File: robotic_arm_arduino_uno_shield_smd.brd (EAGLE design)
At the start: 44.5 x 53.3 mm, 39 parts, among them J1 (ID,OD)=(2.1,5.5)MM

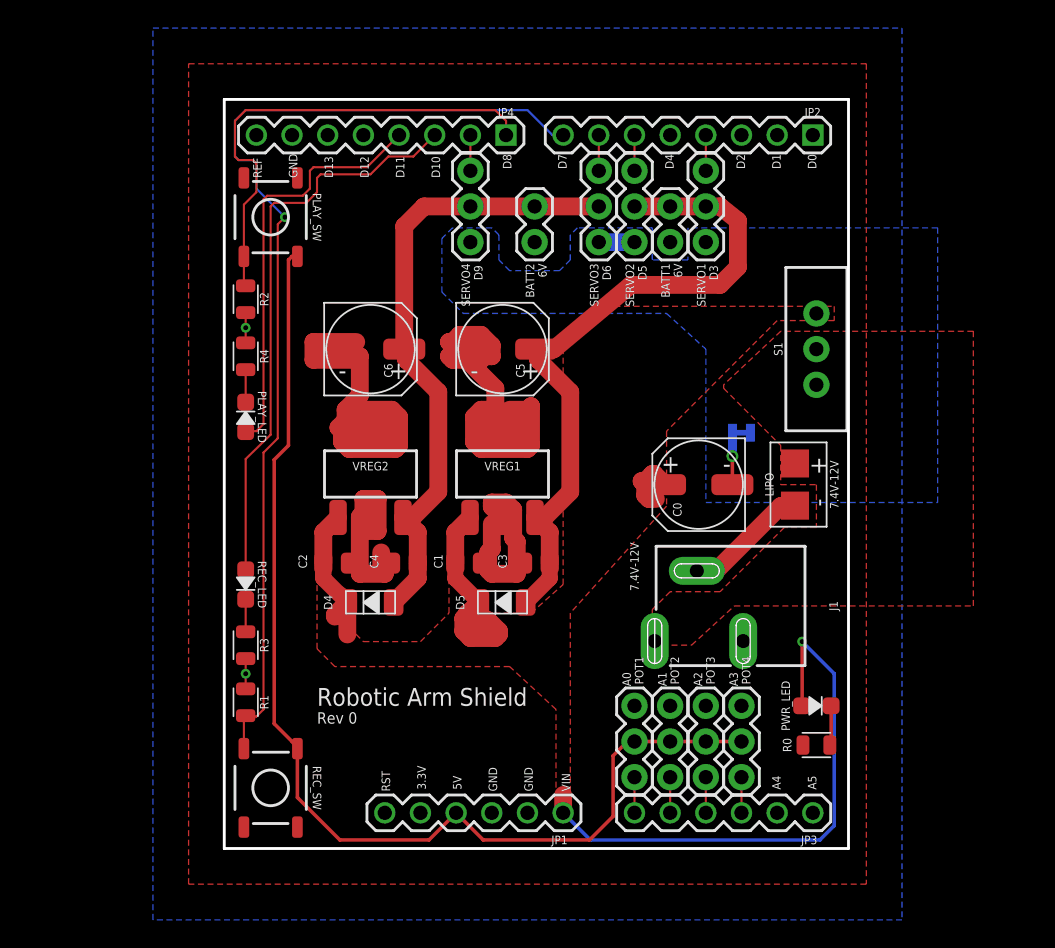
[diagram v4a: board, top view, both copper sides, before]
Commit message: Rev 2.  Changed pad sizes of 805 SMD components.
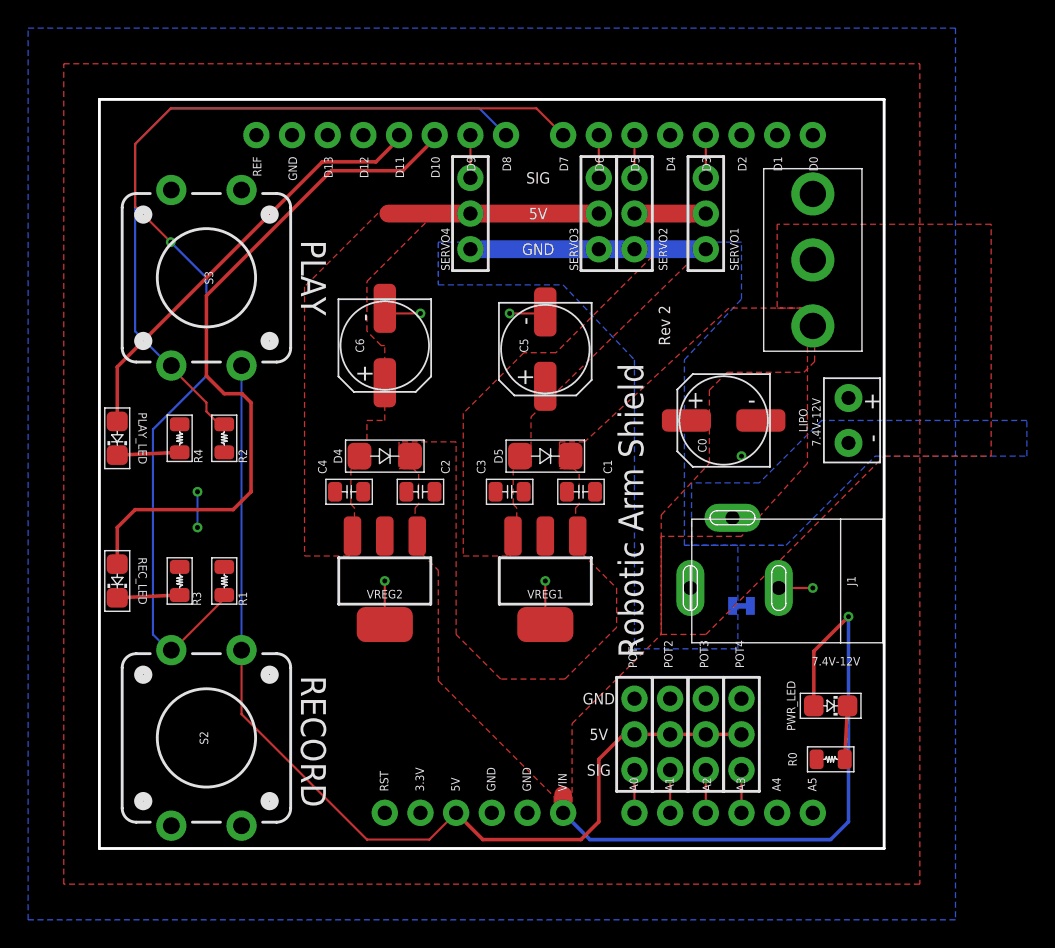
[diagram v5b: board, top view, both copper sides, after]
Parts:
- removed BATT1, BATT2: 6V, SparkFun-Connectors:1X02
- removed JP1: Power, SparkFun:1X06
- removed JP2: Digital1, SparkFun:1X08
- removed JP3: Analog, SparkFun:1X06
- removed JP4: Digital2, SparkFun:1X08
- removed PLAY_SW, REC_SW: TACTILE-SW_500mA/12V, MrSwirlyEyes:SW_MOMENTARY_SPST-NO_SMD_12V_50MA_5.2MM
- added J2, J3: 1x06-VERT-MALE, connectors:1X06-VERT-MALE
- added J4, J5: 1x08-VERT-MALE, connectors:1X08-VERT-MALE
- added S2, S3: MOMENTARY-SWITCH-SPST-PTH-12MM, SparkFun-Switches:TACTILE_SWITCH_PTH_12MM
- C0, C5, C6: device MrSwirlyEyes:CAP_POL_ALUM-ELECTROLYTIC -> MrSwirlyEyes:CAP_POL_SMD_L6.6-W6.6
- LIPO: value BATTERY -> BATTERYPTH_HOLES; device MrSwirlyEyes:DUAL_SMD_PADS -> MrSwirlyEyes:DUAL_PTH_PADS
- POT1, POT2, POT3, POT4: value 22K -> 1x03-VERT-FEMALE; device SparkFun-Connectors:1X03 -> connectors:1X03-VERT-FEMALE
- S1: device SparkFun-Switches:SWITCH_SPDT_PTH_11.6X4.0MM -> MrSwirlyEyes:SW-SLIDE_SPDT_5A-28V_13L-7W
- SERVO1, SERVO2, SERVO3, SERVO4: value (none) -> 1x03-VERT-FEMALE; device SparkFun-Connectors:1X03 -> connectors:1X03-VERT-FEMALE
- moved SUPPLY14 12.3 mm to (36.8, 17.3), turned to 270 degrees
- moved D5 10.9 mm to (22.9, 27.9), turned to 0 degrees
- moved D4 10.5 mm to (11.4, 27.9), turned to 0 degrees
- moved R2 10.0 mm to (0.00, 29.2)
- moved C1 9.48 mm to (25.4, 25.4), turned to 180 degrees
- moved PLAY_LED 9.27 mm to (-7.62, 29.2), turned to 270 degrees
- moved REC_LED 9.15 mm to (-7.62, 19.1)
- moved R1 8.77 mm to (0.00, 19.1)
- moved VREG1 8.21 mm to (22.9, 19.1), turned to 180 degrees
- moved C2 7.84 mm to (14.0, 25.4), turned to 180 degrees
- moved VREG2 7.69 mm to (11.4, 19.1), turned to 180 degrees
- moved R4 7.50 mm to (-3.17, 29.2)
- moved R3 6.56 mm to (-3.17, 19.1), turned to 270 degrees
- moved C4 6.43 mm to (8.89, 25.4), turned to 0 degrees
- moved S1 6.36 mm to (41.9, 41.9), turned to 90 degrees
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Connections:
- removed net N$6: J1.GND@2, LIPO.V-
- removed net VBATT: J1.PWR, LIPO.V+, S1.2
- new net +: J1.PWR, LIPO.+, S1.P$2
- new net -: J1.GND@2, LIPO.-
- net 3.3V: now also J2.2; no longer JP1.2
- net 5V: now also J2.3, S2.1, S3.3; no longer JP1.3, PLAY_SW.3, REC_SW.1
- net A0: now also J3.6; no longer JP3.6
- net A1: now also J3.5; no longer JP3.5
- net A2: now also J3.4; no longer JP3.4
- net A3: now also J3.3; no longer JP3.3
- net A4: now also J3.2; no longer JP3.2
- net A5: now also J3.1; no longer JP3.1
- net AREF: now also J5.8; no longer JP4.8
- net D10: now also J5.3; no longer JP4.3
- net D11: now also J5.4; no longer JP4.4
- net D12: now also J5.5; no longer JP4.5
- net D13: now also J5.6; no longer JP4.6
- net D2: now also J4.3; no longer JP2.3
- net D3: now also J4.4; no longer JP2.4
- net D4: now also J4.5; no longer JP2.5
- net D5: now also J4.6; no longer JP2.6
- net D6: now also J4.7; no longer JP2.7
- net D7: now also J4.8, S2.3; no longer JP2.8, REC_SW.3
- net D8: now also J5.1, S3.1; no longer JP4.1, PLAY_SW.1
- net D9: now also J5.2; no longer JP4.2
- net GND: now also J2.4, J2.5, J5.7; no longer BATT1.2, BATT2.2, JP1.4, JP1.5, JP4.7
- net RESET: now also J2.1; no longer JP1.1
- net RX: now also J4.1; no longer JP2.1
- net TX: now also J4.2; no longer JP2.2
- net VCC_1: no longer BATT1.1
- net VCC_2: no longer BATT2.1
- net VIN: now also J2.6, S1.P$1; no longer JP1.6, S1.1
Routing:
- net GND: track 91.0 -> 17.3 mm, vias 3 -> 8
- net VCC_1: track 49.2 -> 5.08 mm
- net VCC_2: track 44.8 -> 15.0 mm
- net VIN: track 73.5 -> 44.9 mm
- net D8: track 34.6 -> 51.5 mm
- net NGND: track 2.54 -> 16.8 mm
- net D10: track 41.0 -> 50.4 mm
- net N$6: track 8.91 -> 0.00 mm
- net 5V: track 80.0 -> 71.6 mm
- net D7: track 72.9 -> 78.4 mm
- net N$2: track 2.31 -> 4.45 mm
- net N$1: track 2.31 -> 4.45 mm
- net D11: track 29.8 -> 30.9 mm
- net N$4: track 2.81 -> 3.82 mm
- net A3: track 2.54 -> 3.05 mm
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- added copper zone on layer 1, net +
- added copper zone on layer 16, net -
- added copper zone on layer 1, net VCC_1
- added copper zone on layer 1, net VCC_2
- removed copper zone on layer 1, net VBATT
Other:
- board size 44.5 x 53.3 mm -> 55.9 x 53.3 mm
- board text added: "PLAY"
- board text added: "RECORD"
- board text added: "Rev 2"
- board text added: "Rev 2 Designed by: Buu Truong CADed by: MrSwirlyEyes"
- board text added: "SIG"
- board text removed: "6V"
- board text removed: "CADed by: MrSwirlyEyes"
- board text removed: "Designed by: Buu Truong"
- board text removed: "Rev 0"

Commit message: Added switch object parameters for power switch and PLAY,RECORD buttons.  Added potentiometer from digikey to POT object.  Added Servo from Amazon to SERVO object MG90S
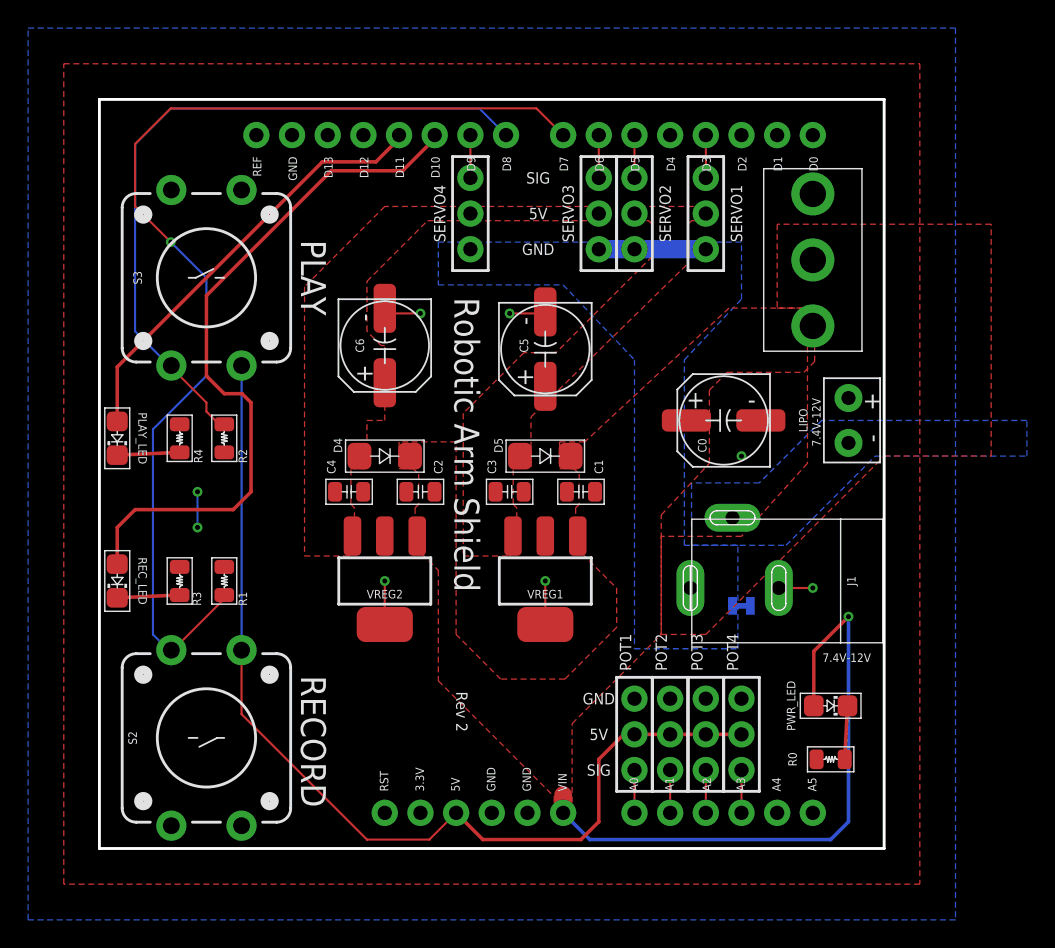
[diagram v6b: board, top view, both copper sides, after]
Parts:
- POT1, POT2, POT3, POT4: value 1x03-VERT-FEMALE -> 20KΩ; device connectors:1X03-VERT-FEMALE -> MrSwirlyEyes:CONNECTOR_POTENTIOMETER_NO-MARKINGS_FEMALE-HEADER
- R3: value 10KΩ -> 2KΩ
- R4: value 10KΩ -> 1KΩ
- S1: value (none) -> 5A/28V
- S2, S3: value MOMENTARY-SWITCH-SPST-PTH-12MM -> (none); device SparkFun-Switches:TACTILE_SWITCH_PTH_12MM -> MrSwirlyEyes:SPST-PTH-12MM
- SERVO1, SERVO2, SERVO3, SERVO4: value 1x03-VERT-FEMALE -> MG90S; device connectors:1X03-VERT-FEMALE -> MrSwirlyEyes:CONNECTOR_SERVO_NO-MARKINGS
- turned POT1 to 90 degrees
- turned POT2 to 90 degrees
- turned POT3 to 90 degrees
- turned POT4 to 90 degrees
- turned SERVO1 to 270 degrees
- turned SERVO2 to 270 degrees
- turned SERVO3 to 270 degrees
- turned SERVO4 to 270 degrees
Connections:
- net 5V: now also POT1.CCW, POT2.CCW, POT3.CCW, POT4.CCW; no longer POT1.2, POT2.2, POT3.2, POT4.2
- net A0: now also POT1.S; no longer POT1.3
- net A1: now also POT2.S; no longer POT2.3
- net A2: now also POT3.S; no longer POT3.3
- net A3: now also POT4.S; no longer POT4.3
- net D3: now also SERVO1.1; no longer SERVO1.3
- net D5: now also SERVO2.1; no longer SERVO2.3
- net D6: now also SERVO3.1; no longer SERVO3.3
- net D9: now also SERVO4.1; no longer SERVO4.3
- net GND: now also POT1.CW, POT2.CW, POT3.CW, POT4.CW; no longer POT1.1, POT2.1, POT3.1, POT4.1
- net NGND: now also SERVO1.3, SERVO2.3, SERVO3.3, SERVO4.3; no longer SERVO1.1, SERVO2.1, SERVO3.1, SERVO4.1
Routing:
- net VCC_2: track 15.0 -> 0.00 mm
- net VCC_1: track 5.08 -> 0.00 mm
- net NGND: track 16.8 -> 15.2 mm

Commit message: Rev 2.  Modified board and schematic for new parts
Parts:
- S2, S3: value (none) -> 50mA/12V
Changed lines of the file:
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@@
 <attribute name="VALUE" value="5A/28V" x="41.91" y="41.91" size="1.778" layer="27" rot="R90" display="off"/>
 </element>
-<element name="S2" library="MrSwirlyEyes" package="SPST-PTH-12MM" value="" x="-1.27" y="7.874" smashed="yes" rot="R90">
+<element name="S2" library="MrSwirlyEyes" package="SPST-PTH-12MM" value="50mA/12V" x="-1.27" y="7.874" smashed="yes" rot="R90">
+<attribute name="CREATOR" value="MrSwirlyEyes" x="-1.27" y="7.874" size="1.778" layer="27" rot="R90" display="off"/>
+<attribute name="DATASHEET" value="https://www.sparkfun.com/datasheets/Components/Buttons/TSA12110%20TACT%20SWITCH.jpg" x="-1.27" y="7.874" size="1.778" layer="27" rot="R90" display="off"/>
+<attribute name="DIST" value="Sparkfun" x="-1.27" y="7.874" size="1.778" layer="27" rot="R90" display="off"/>
+<attribute name="DISTLINK" value="https://www.sparkfun.com/products/10302" x="-1.27" y="7.874" size="1.778" layer="27" rot="R90" display="off"/>
+<attribute name="DISTPN" value="COM-10302" x="-1.27" y="7.874" size="1.778" layer="27" rot="R90" display="off"/>
+<attribute name="MFR" value="" x="-1.27" y="7.874" size="1.778" layer="27" rot="R90" display="off"/>
+<attribute name="MPN" value="" x="-1.27" y="7.874" size="1.778" layer="27" rot="R90" display="off"/>
 <attribute name="NAME" x="-6.223" y="7.874" size="0.6096" layer="25" font="vector" ratio="20" rot="R90" align="bottom-center"/>
+<attribute name="VALUE" value="50mA/12V" x="-1.27" y="7.874" size="1.778" layer="27" rot="R90" display="off"/>
 </element>
-<element name="S3" library="MrSwirlyEyes" package="SPST-PTH-12MM" value="" x="-1.27" y="40.64" smashed="yes" rot="R270">
+<element name="S3" library="MrSwirlyEyes" package="SPST-PTH-12MM" value="50mA/12V" x="-1.27" y="40.64" smashed="yes" rot="R270">
+<attribute name="CREATOR" value="MrSwirlyEyes" x="-1.27" y="40.64" size="1.778" layer="27" rot="R270" display="off"/>
+<attribute name="DATASHEET" value="https://www.sparkfun.com/datasheets/Components/Buttons/TSA12110%20TACT%20SWITCH.jpg" x="-1.27" y="40.64" size="1.778" layer="27" rot="R270" display="off"/>
+<attribute name="DIST" value="Sparkfun" x="-1.27" y="40.64" size="1.778" layer="27" rot="R270" display="off"/>
+<attribute name="DISTLINK" value="https://www.sparkfun.com/products/10302" x="-1.27" y="40.64" size="1.778" layer="27" rot="R270" display="off"/>
+<attribute name="DISTPN" value="COM-10302" x="-1.27" y="40.64" size="1.778" layer="27" rot="R270" display="off"/>
+<attribute name="MFR" value="" x="-1.27" y="40.64" size="1.778" layer="27" rot="R270" display="off"/>
+<attribute name="MPN" value="" x="-1.27" y="40.64" size="1.778" layer="27" rot="R270" display="off"/>
 <attribute name="NAME" x="-6.477" y="40.64" size="0.6096" layer="25" font="vector" ratio="20" rot="R270" align="bottom-center"/>
+<attribute name="VALUE" value="50mA/12V" x="-1.27" y="40.64" size="1.778" layer="27" rot="R270" display="off"/>
 </element>
 <element name="SERVO1" library="MrSwirlyEyes" package="CONNECTOR_SERVO_NO-MARKINGS" value="MG90S" x="34.29" y="45.212" smashed="yes" rot="R270">

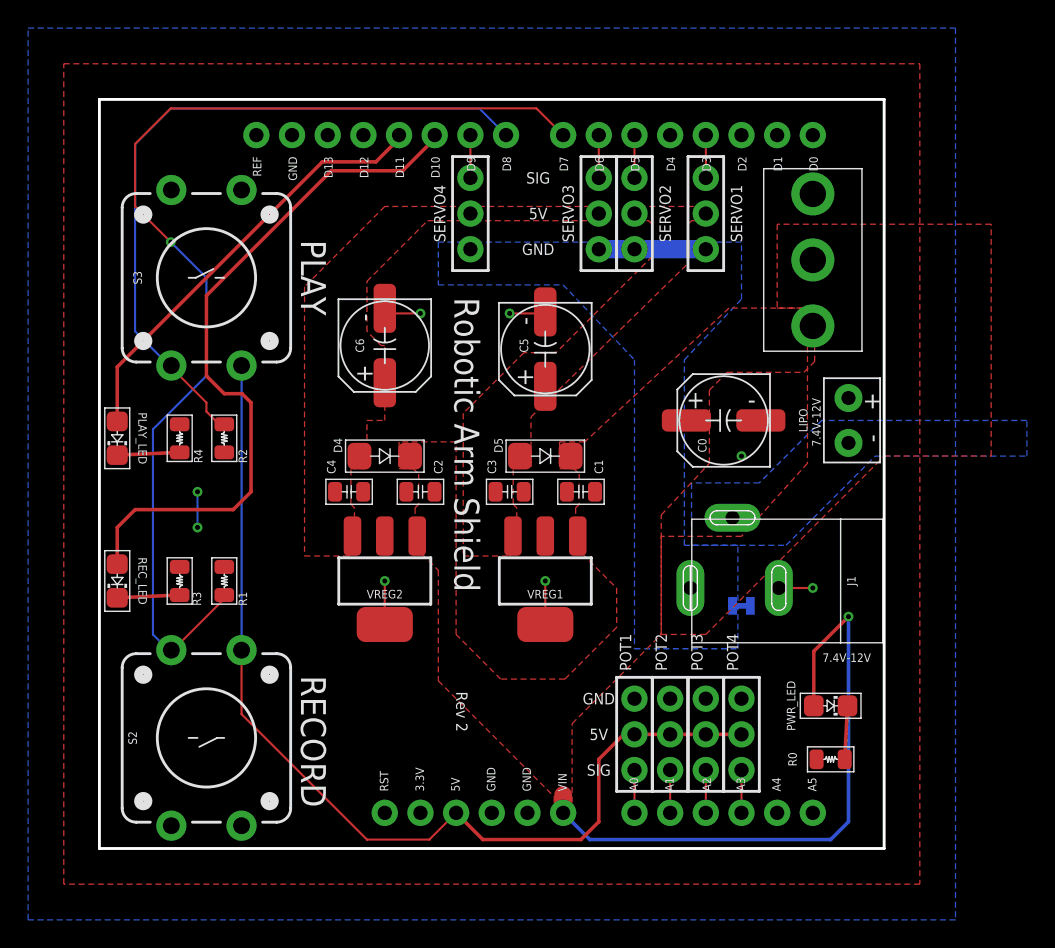
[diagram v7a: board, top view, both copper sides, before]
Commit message: Rev 3:  Complete revamp.  Replaced the (2) 1A/5V VREGs for (1) 5A/5V VREG
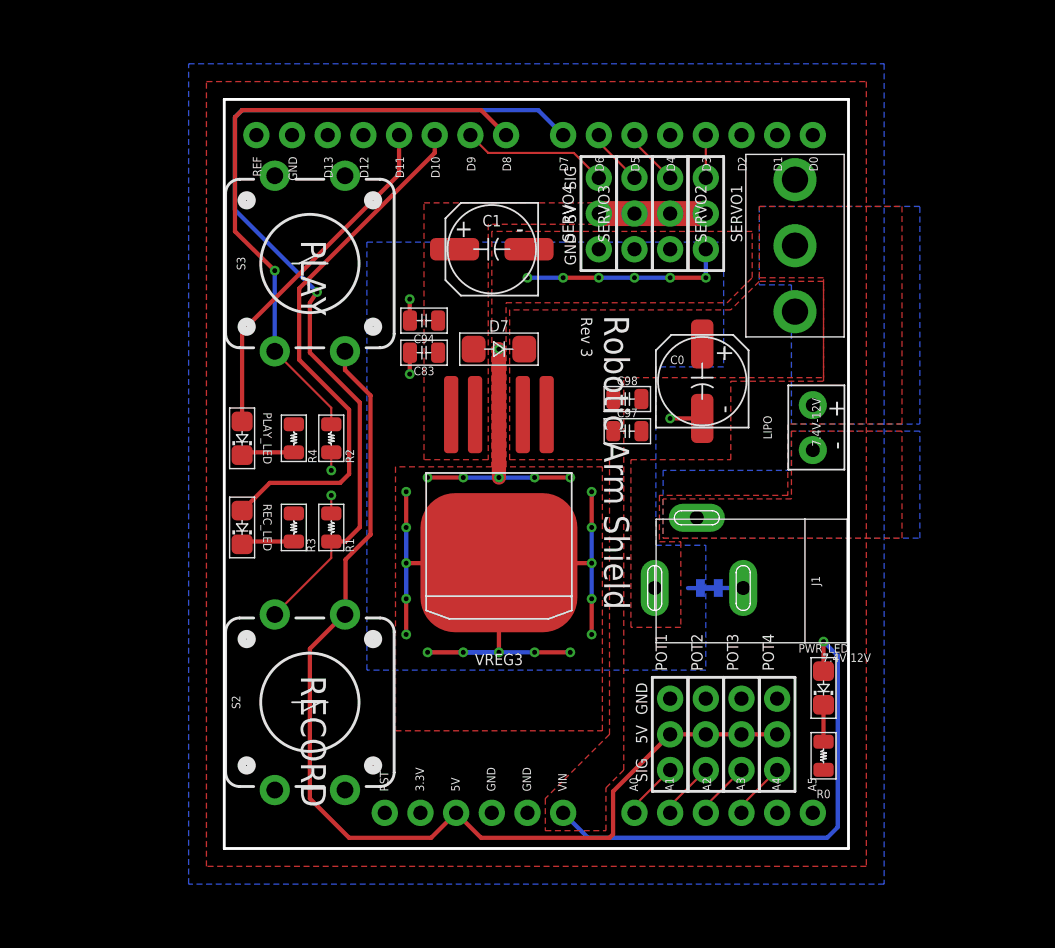
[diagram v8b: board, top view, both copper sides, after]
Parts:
- removed C2: 0.22uF/50V, MrSwirlyEyes:CAP_CER_SMD-805
- removed C3, C4: 0.1uF/50V, MrSwirlyEyes:CAP_CER_SMD-805
- removed C5, C6: 100UF/16V, MrSwirlyEyes:CAP_POL_SMD_L6.6-W6.6
- removed D4, D5: 1A/50V, MrSwirlyEyes:DIODE_SMD_1A-50V-SOD123F
- removed VREG1, VREG2: 1.5A/5V, MrSwirlyEyes:SOT223
- added C83, C98: 0.1uF/50V, MrSwirlyEyes:CAP_CER_SMD-805
- added C94, C97: 10uF/25V, MrSwirlyEyes:CAP_CER_SMD-805
- added D7: 1A/50V, MrSwirlyEyes:DIODE_SMD_1A-50V-SOD123F
- added VREG3: 5A/5V, MrSwirlyEyes:TO-263-5
- C1: value 0.22uF/50V -> 100UF/16V; device MrSwirlyEyes:CAP_CER_SMD-805 -> MrSwirlyEyes:CAP_POL_SMD_L6.6-W6.6
- R0, R1, R2, R3, R4: device MrSwirlyEyes:RESC2012X60_HS -> MrSwirlyEyes:RESISTOR_SMD-805
- moved C1 18.4 mm to (19.1, 42.7), turned to 0 degrees
- moved REC_LED 9.67 mm to (1.27, 22.9)
- moved SERVO4 9.14 mm to (26.7, 45.2)
- moved R3 8.98 mm to (4.95, 22.9)
- moved PLAY_LED 8.89 mm to (1.27, 29.2)
- moved R1 8.52 mm to (7.62, 22.9)
- moved R4 8.13 mm to (4.95, 29.2)
- moved S2 7.79 mm to (6.10, 10.4)
- moved R2 7.62 mm to (7.62, 29.2)
- moved S3 7.44 mm to (6.10, 41.7)
- moved C0 3.18 mm to (34.0, 33.3), turned to 270 degrees
- moved SUPPLY14 2.62 mm to (34.5, 18.6)
- moved LIPO 2.59 mm to (41.9, 30.0)
- moved J1 2.54 mm to (36.8, 19.1)
- moved POT1 2.54 mm to (31.8, 8.13)
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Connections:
- removed net VCC_1: C3.1, C5.A, D5.A, SERVO1.2, SERVO2.2, VREG1.3
- removed net VCC_2: C4.1, C6.A, D4.A, SERVO3.2, SERVO4.2, VREG2.3
- new net VCC: C1.A, C83.1, C94.1, D7.A, SERVO1.2, SERVO2.2, SERVO3.2, SERVO4.2, VREG3.4
- net GND: now also C97.2, C98.2; no longer C1.2, C2.2, C3.2, C4.2, C5.K, C6.K, VREG1.2, VREG1.4, VREG2.2, VREG2.4
- net NGND: now also C1.K, C83.2, C94.2, VREG3.3, VREG3.TAB
- net VIN: now also C97.1, C98.1, D7.K, VREG3.1, VREG3.2; no longer C1.1, C2.1, D4.K, D5.K, VREG1.1, VREG2.1
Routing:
- net NGND: track 15.2 -> 93.2 mm, vias 0 -> 29
- net D10: track 50.4 -> 38.3 mm
- net D7: track 78.4 -> 66.9 mm
- net GND: track 17.3 -> 6.63 mm, vias 8 -> 3
- net VIN: track 44.9 -> 36.3 mm
- net VCC: track 0.00 -> 7.62 mm
- net D9: track 3.05 -> 10.4 mm
- net D8: track 51.5 -> 45.0 mm, vias 0 -> 1
- net D11: track 30.9 -> 25.0 mm
- net 5V: track 71.6 -> 75.2 mm
- net N$4: track 3.82 -> 2.63 mm
- net D6: track 3.05 -> 4.10 mm
- net D5: track 3.05 -> 4.10 mm
- net A3: track 3.05 -> 4.10 mm
- net A2: track 3.05 -> 4.10 mm
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- added copper zone on layer 16, net +
- added copper zone on layer 1, net -
- added copper zone on layer 1, net NGND
- added copper zone on layer 1, net VCC
- removed copper zone on layer 1, net VCC_1
- removed copper zone on layer 1, net VCC_2
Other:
- board size 55.9 x 53.3 mm -> 44.5 x 53.3 mm
- board text added: "Rev 3"
- board text added: "Rev 3 Designed by: Buu Truong CADed by: MrSwirlyEyes"
- board text removed: "1A/50V"
- board text removed: "Rev 2"
- board text removed: "Rev 2 Designed by: Buu Truong CADed by: MrSwirlyEyes"
